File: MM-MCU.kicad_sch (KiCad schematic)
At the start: 17 parts, among them U5 STM32F205RGTx

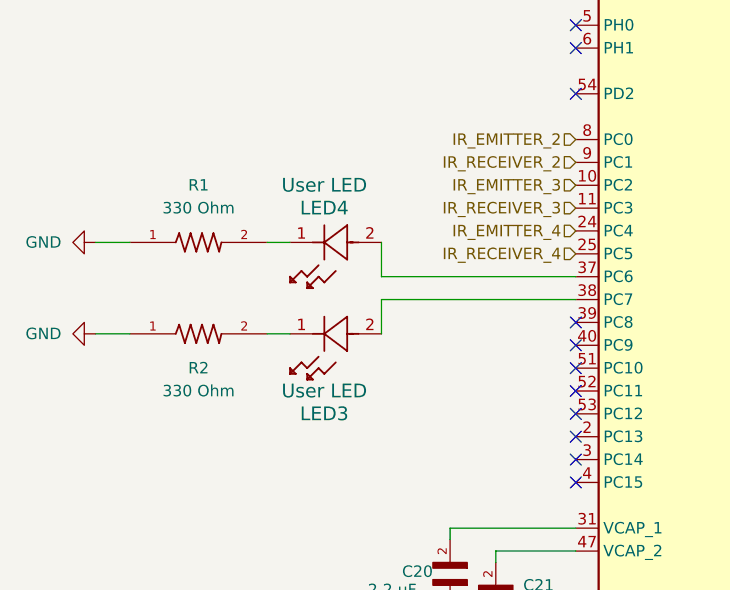
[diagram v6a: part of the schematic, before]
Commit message: LED changes, mosfet footprint fixed
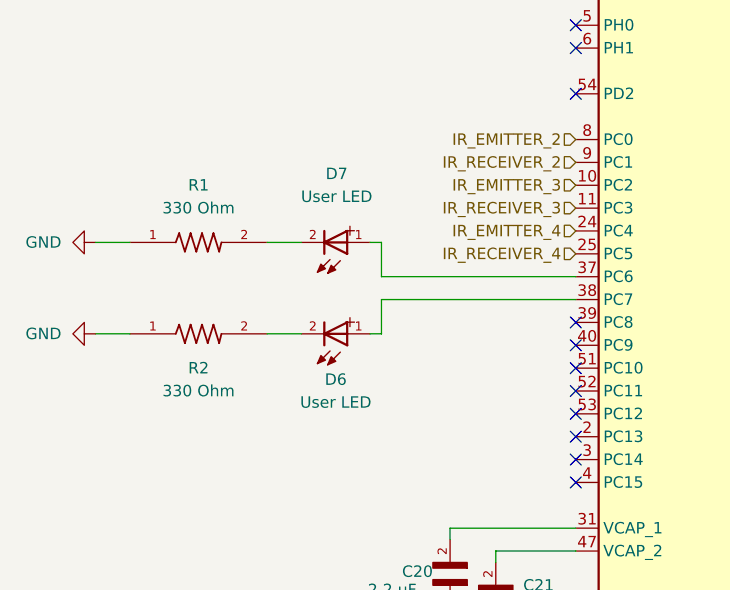
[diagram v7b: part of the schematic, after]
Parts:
- removed LED3, LED4: User LED, symbol UserLED_2026-01-27_18-27-04:LTL-4231N
- added D6, D7: User LED, LED_WL-TMRC_5MM:WL-TMRC_5MM, symbol PowerIndicatorLED_WL-TMRC_5MM:WL-TMRC_5MM
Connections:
- net at R2.2: now also D6.2
- net at U5.38 (PC7): now also D6.1
- net at R1.2: now also D7.2
- net at U5.37 (PC6): now also D7.1
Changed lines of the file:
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@@
 	(wire
 		(pts
+			(xy 57.15 121.92) (xy 60.96 121.92)
+		)
+		(stroke
+			(width 0)
+			(type default)
+		)
+	)
+	(wire
+		(pts
 			(xy 82.55 92.71) (xy 91.44 92.71)
 		)
@@
 	(wire
 		(pts
-			(xy 99.06 48.26) (xy 100.33 48.26)
+			(xy 68.58 121.92) (xy 69.85 121.92)
 		)
 		(stroke
@@
 	(wire
 		(pts
-			(xy 57.15 132.08) (xy 59.69 132.08)
+			(xy 99.06 48.26) (xy 100.33 48.26)
 		)
 		(stroke
@@
 	(wire
 		(pts
-			(xy 113.03 27.94) (xy 114.3 27.94)
+			(xy 57.15 132.08) (xy 60.96 132.08)
 		)
 		(stroke
@@
 	(wire
 		(pts
-			(xy 116.84 68.58) (xy 118.11 68.58)
+			(xy 113.03 27.94) (xy 114.3 27.94)
 		)
 		(stroke
@@
 	(wire
 		(pts
-			(xy 69.85 125.73) (xy 91.44 125.73)
+			(xy 116.84 68.58) (xy 118.11 68.58)
 		)
 		(stroke
@@
 	(wire
 		(pts
-			(xy 101.6 38.1) (xy 102.87 38.1)
+			(xy 69.85 125.73) (xy 91.44 125.73)
 		)
 		(stroke
@@
 	(wire
 		(pts
-			(xy 69.85 128.27) (xy 69.85 132.08)
+			(xy 101.6 38.1) (xy 102.87 38.1)
 		)
 		(stroke
@@
 	(wire
 		(pts
-			(xy 116.84 80.01) (xy 116.84 82.55)
+			(xy 69.85 128.27) (xy 69.85 132.08)
 		)
 		(stroke
@@
 	(wire
 		(pts
-			(xy 69.85 121.92) (xy 69.85 125.73)
+			(xy 116.84 80.01) (xy 116.84 82.55)
 		)
 		(stroke
@@
 	(wire
 		(pts
-			(xy 57.15 121.92) (xy 59.69 121.92)
-		)
-		(stroke
-			(width 0)
-			(type default)
-		)
-	)
-	(wire
-		(pts
 			(xy 116.84 67.31) (xy 116.84 68.58)
 		)
@@
 	(wire
 		(pts
+			(xy 68.58 132.08) (xy 69.85 132.08)
+		)
+		(stroke
+			(width 0)
+			(type default)
+		)
+	)
+	(wire
+		(pts
 			(xy 110.49 176.53) (xy 110.49 177.8)
 		)
@@
 	(wire
 		(pts
+			(xy 69.85 121.92) (xy 69.85 125.73)
+		)
+		(stroke
+			(width 0)
+			(type default)
+		)
+	)
+	(wire
+		(pts
 			(xy 111.76 38.1) (xy 111.76 82.55)
 		)
@@
 	)
 	(symbol
-		(lib_id "UserLED_2026-01-27_18-27-04:LTL-4231N")
-		(at 69.85 132.08 180)
-		(unit 1)
-		(exclude_from_sim no)
-		(in_bom yes)
-		(on_board yes)
-		(dnp no)
-		(property "Reference" "LED3"
-			(at 63.5 140.97 0)
-			(effects
-				(font
-					(size 1.524 1.524)
-				)
-			)
-		)
-		(property "Value" "User LED"
-			(at 63.5 138.43 0)
-			(effects
-				(font
-					(size 1.524 1.524)
-				)
-			)
-		)
-		(property "Footprint" ""
-			(at 69.85 132.08 0)
-			(effects
-				(font
-					(size 1.27 1.27)
-					(italic yes)
-				)
-				(hide yes)
-			)
-		)
-		(property "Datasheet" "LTL-4231N"
-			(at 69.85 132.08 0)
-			(effects
-				(font
-					(size 1.27 1.27)
-					(italic yes)
-				)
-				(hide yes)
-			)
-		)
-		(property "Description" ""
-			(at 69.85 132.08 0)
-			(effects
-				(font
-					(size 1.27 1.27)
-				)
-				(hide yes)
-			)
-		)
-		(pin "1"
-		)
-		(pin "2"
-		)
-		(instances
-			(project "IREmitter"
-				(path "/d311851a-8b0b-4acf-b2e7-1b968b2adbe7/2e1dc814-2c57-413c-a832-0cf6350c5f62"
-					(reference "LED3")
-					(unit 1)
-				)
-			)
-		)
-	)
-	(symbol
 		(lib_id "1µFCapacitor_CL10B105KP8NNNC:CL10B105KP8NNNC")
 		(at 120.65 68.58 0)
@@
 	)
 	(symbol
-		(lib_id "UserLED_2026-01-27_18-27-04:LTL-4231N")
-		(at 69.85 121.92 180)
-		(unit 1)
-		(exclude_from_sim no)
-		(in_bom yes)
-		(on_board yes)
-		(dnp no)
-		(property "Reference" "LED4"
-			(at 63.5 118.11 0)
-			(effects
-				(font
-					(size 1.524 1.524)
-				)
-			)
-		)
-		(property "Value" "User LED"
-			(at 63.5 115.57 0)
-			(effects
-				(font
-					(size 1.524 1.524)
-				)
-			)
-		)
-		(property "Footprint" ""
-			(at 69.85 121.92 0)
-			(effects
-				(font
-					(size 1.27 1.27)
-					(italic yes)
-				)
-				(hide yes)
-			)
-		)
-		(property "Datasheet" "LTL-4231N"
-			(at 69.85 121.92 0)
-			(effects
-				(font
-					(size 1.27 1.27)
-					(italic yes)
-				)
-				(hide yes)
-			)
-		)
-		(property "Description" ""
-			(at 69.85 121.92 0)
-			(effects
-				(font
-					(size 1.27 1.27)
-				)
-				(hide yes)
-			)
-		)
-		(pin "1"
-		)
-		(pin "2"
-		)
-		(instances
-			(project "IREmitter"
-				(path "/d311851a-8b0b-4acf-b2e7-1b968b2adbe7/2e1dc814-2c57-413c-a832-0cf6350c5f62"
-					(reference "LED4")
-					(unit 1)
-				)
-			)
-		)
-	)
-	(symbol
 		(lib_id "330_ohm_RC0603FR-07330RL:RC0603FR-07330RL")
 		(at 49.53 132.08 0)
@@
 					(unit 1)
 				)
+			)
+		)
+	)
+	(symbol
+		(lib_id "PowerIndicatorLED_WL-TMRC_5MM:WL-TMRC_5MM")
+		(at 63.5 132.08 180)
+		(unit 1)
+		(exclude_from_sim no)
+		(in_bom yes)
+		(on_board yes)
+		(dnp no)
+		(property "Reference" "D6"
+			(at 64.77 137.16 0)
+			(effects
+				(font
+					(size 1.27 1.27)
+				)
+			)
+		)
+		(property "Value" "User LED"
+			(at 64.77 139.7 0)
+			(effects
+				(font
+					(size 1.27 1.27)
+				)
+			)
+		)
+		(property "Footprint" "LED_WL-TMRC_5MM:WL-TMRC_5MM"
+			(at 63.5 132.08 0)
+			(effects
+				(font
+					(size 1.27 1.27)
+				)
+				(justify bottom)
+				(hide yes)
+			)
+		)
+		(property "Datasheet" ""
+			(at 63.5 132.08 0)
+			(effects
+				(font
+					(size 1.27 1.27)
+				)
+				(hide yes)
+			)
+		)
+		(property "Description" ""
+			(at 63.5 132.08 0)
+			(effects
+				(font
+					(size 1.27 1.27)
+				)
+				(hide yes)
+			)
+		)
+		(pin "1"
+		)
+		(pin "2"
+		)
+		(instances
+			(project "IREmitter"
+				(path "/d311851a-8b0b-4acf-b2e7-1b968b2adbe7/2e1dc814-2c57-413c-a832-0cf6350c5f62"
+					(reference "D6")
+					(unit 1)
+				)
+			)
+		)
+	)
+	(symbol
+		(lib_id "PowerIndicatorLED_WL-TMRC_5MM:WL-TMRC_5MM")
+		(at 63.5 121.92 180)
+		(unit 1)
+		(exclude_from_sim no)
+		(in_bom yes)
+		(on_board yes)
+		(dnp no)
+		(fields_autoplaced yes)
+		(property "Reference" "D7"
+			(at 64.8709 114.3 0)
+			(effects
+				(font
+					(size 1.27 1.27)
+				)
+			)
+		)
+		(property "Value" "User LED"
+			(at 64.8709 116.84 0)
+			(effects
+				(font
+					(size 1.27 1.27)
+				)
+			)
+		)
+		(property "Footprint" "LED_WL-TMRC_5MM:WL-TMRC_5MM"
+			(at 63.5 121.92 0)
+			(effects
+				(font
+					(size 1.27 1.27)
+				)
+				(justify bottom)
+				(hide yes)
+			)
+		)
+		(property "Datasheet" ""
+			(at 63.5 121.92 0)
+			(effects
+				(font
+					(size 1.27 1.27)
+				)
+				(hide yes)
+			)
+		)
+		(property "Description" ""
+			(at 63.5 121.92 0)
+			(effects
+				(font
+					(size 1.27 1.27)
+				)
+				(hide yes)
+			)
+		)
+		(pin "1"
+		)
+		(pin "2"
+		)
+		(instances
+			(project "IREmitter"
+				(path "/d311851a-8b0b-4acf-b2e7-1b968b2adbe7/2e1dc814-2c57-413c-a832-0cf6350c5f62"
+					(reference "D7")
+					(unit 1)
+				)
